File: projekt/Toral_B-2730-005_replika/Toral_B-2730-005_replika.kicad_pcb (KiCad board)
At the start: 2 copper layers, 18 parts, among them J1 UKF, J2 Wy

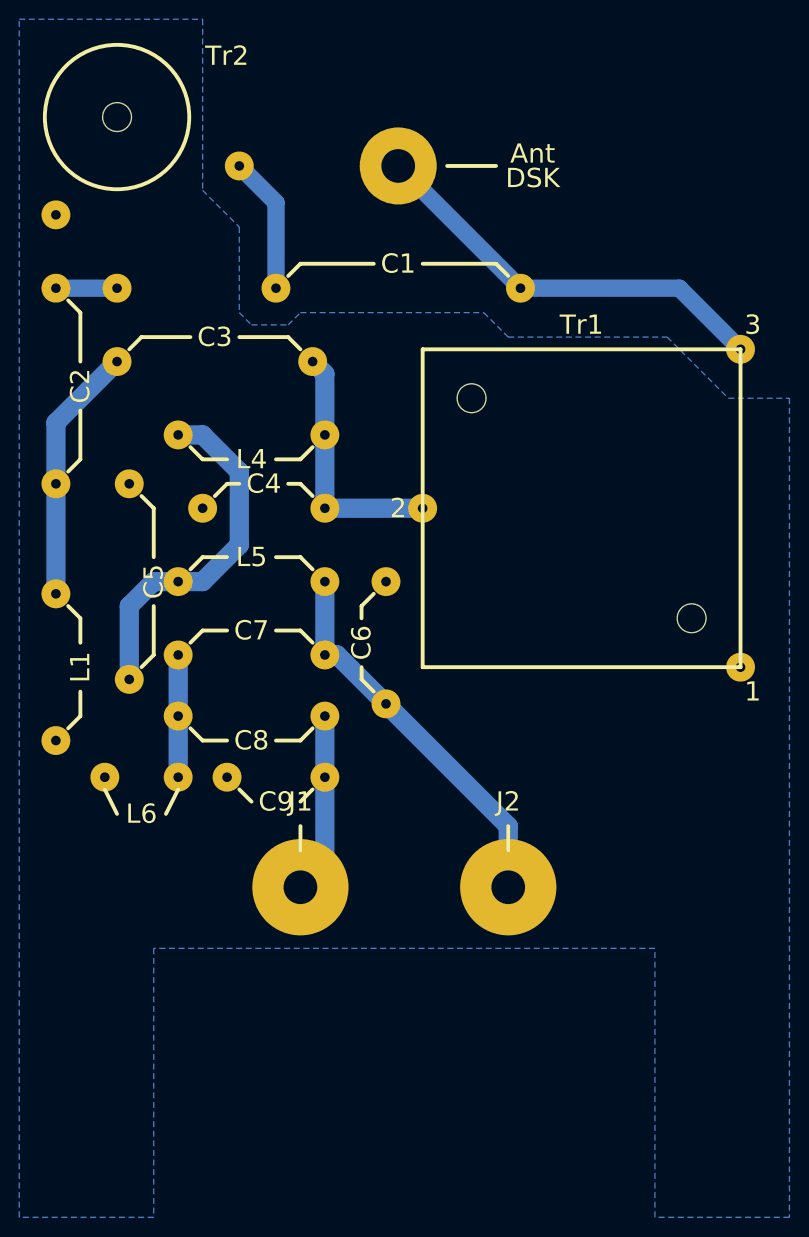
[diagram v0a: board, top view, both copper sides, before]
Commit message: Poprawki w oznaczeniach elementów
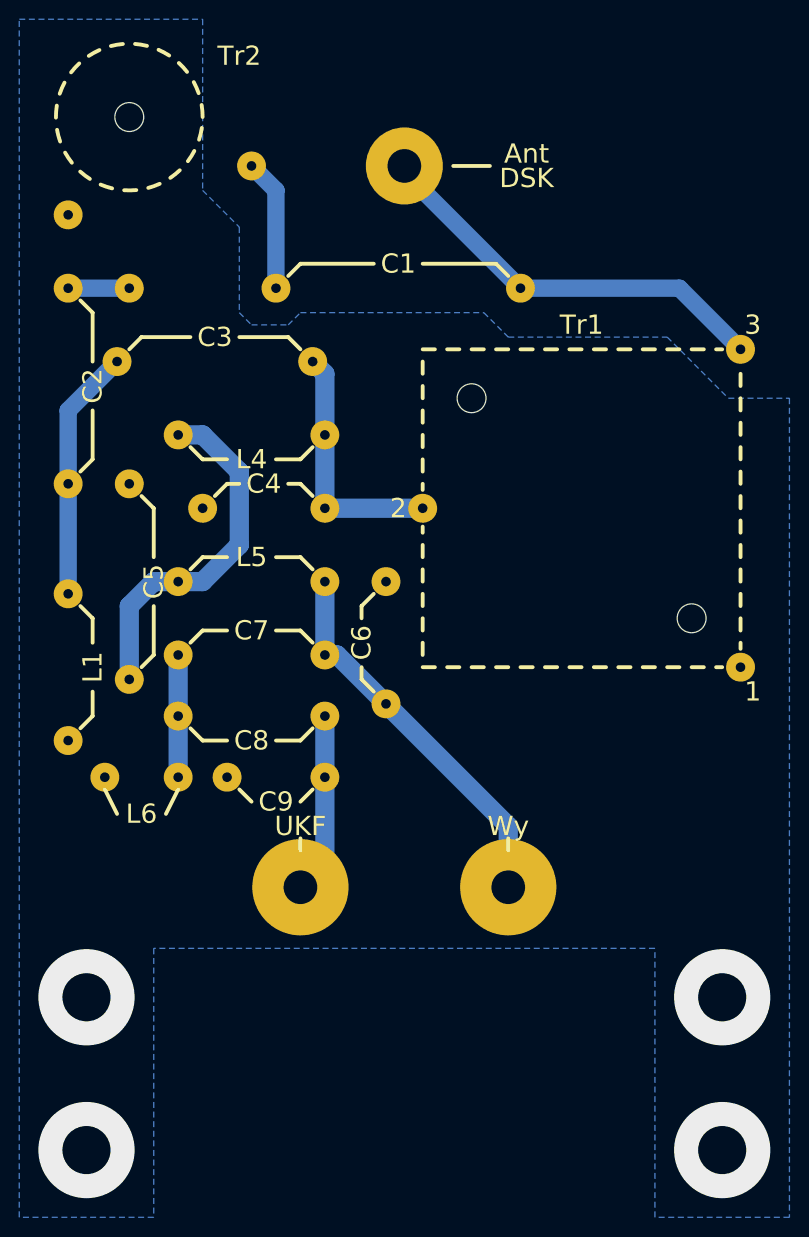
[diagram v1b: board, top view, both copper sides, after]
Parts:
- Tr1: value 36 -> Tr1
- Tr2: value 4.7 -> Tr2
- moved Tr2 1.27 mm to (74.9, 88.9)
- moved C2 1.27 mm to (68.6, 116.8)
- moved L1 1.27 mm to (68.6, 146.1)
- moved AE1 0.63 mm to (103.5, 94.0)
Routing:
- net Net-(C1-Pad1): track 14.3 -> 13.8 mm
- net Net-(C2-Pad2): track 26.8 -> 26.2 mm
- net GND: vias 0 -> 4
